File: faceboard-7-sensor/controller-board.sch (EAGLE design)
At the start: 11 parts

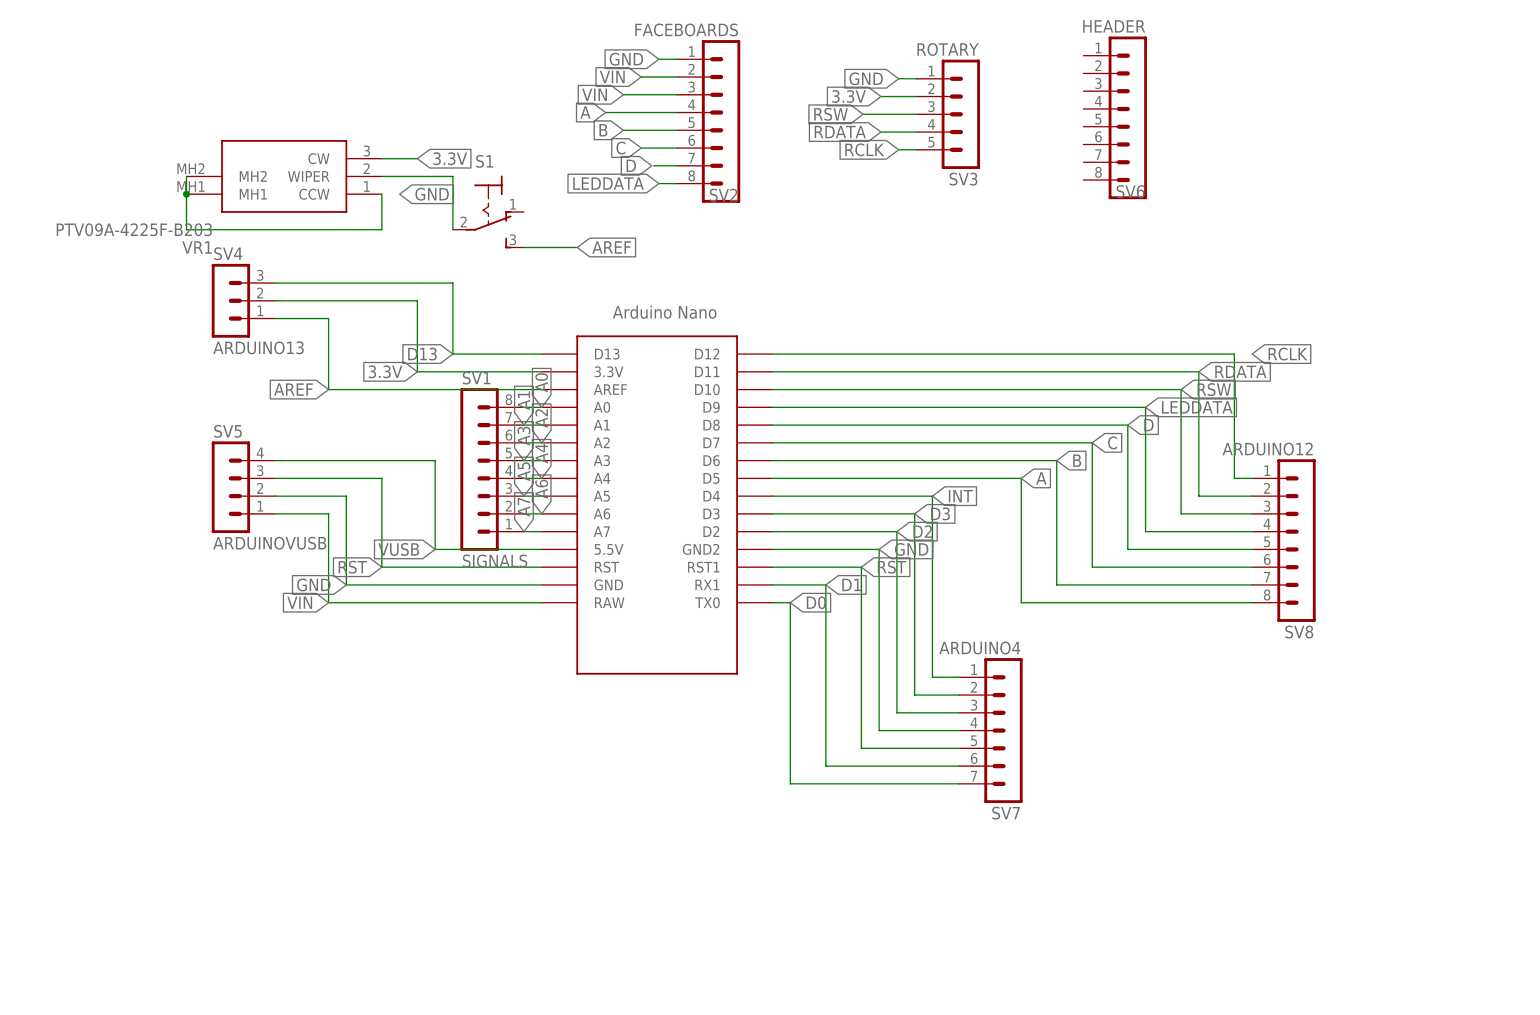
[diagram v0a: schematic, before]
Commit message: add ffc boards
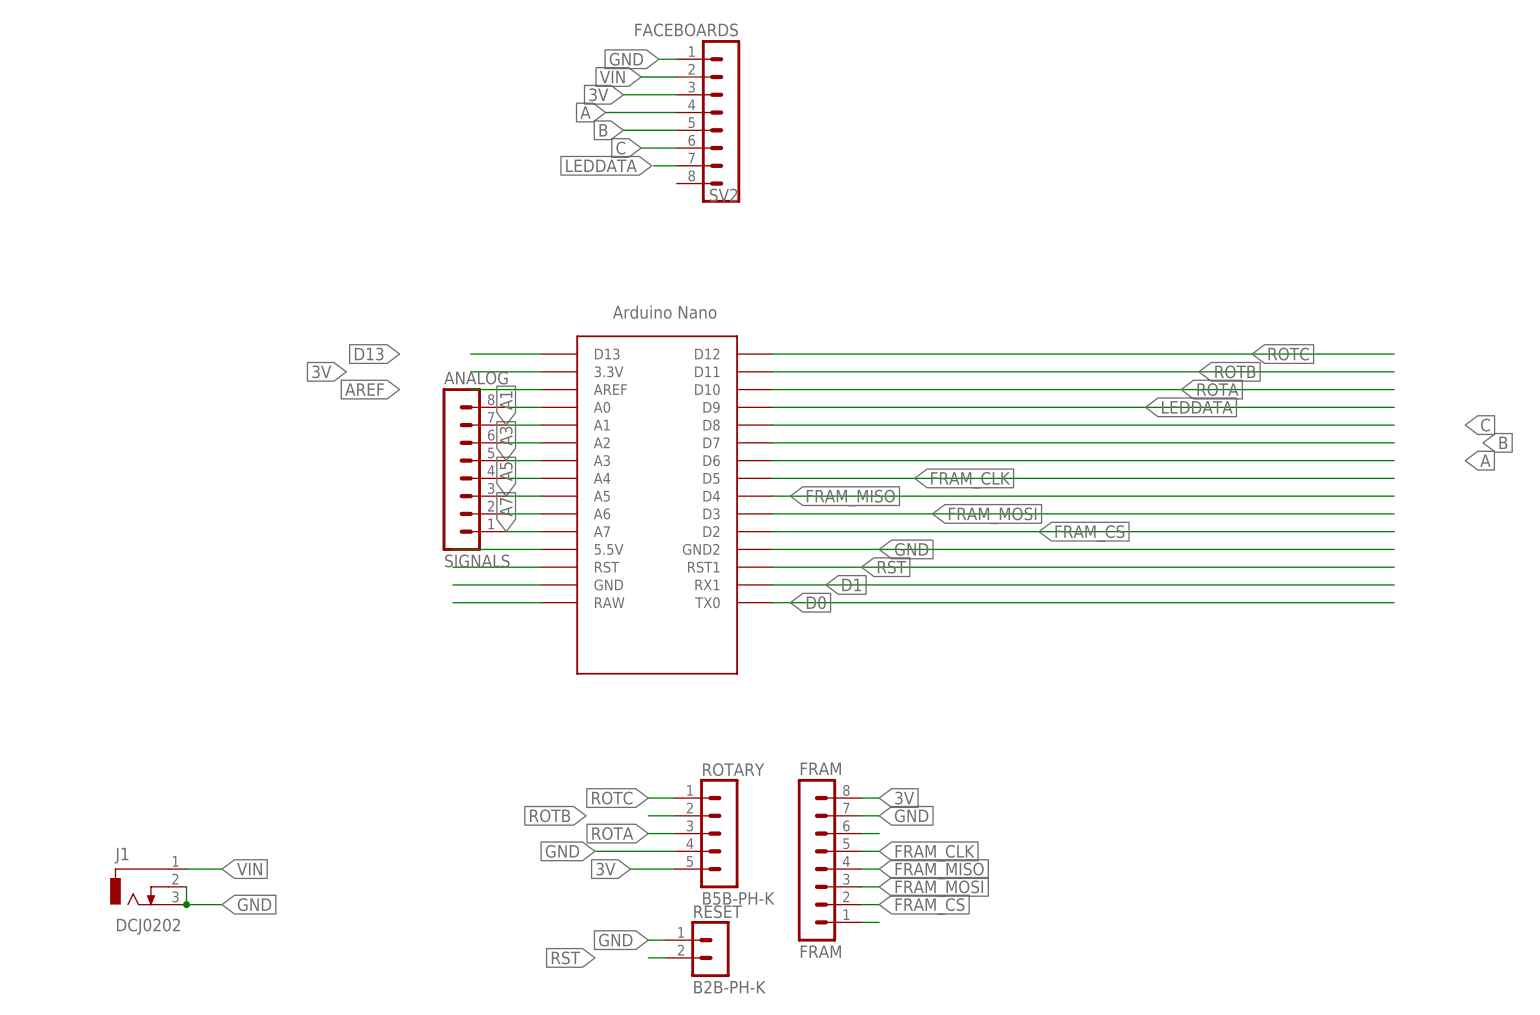
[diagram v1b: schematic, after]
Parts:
- removed S1: (no value), switch:320-916
- removed SV1: SIGNALS, con-lstb:MA08-1
- removed SV3: ROTARY, con-lstb:MA05-1
- removed SV4: ARDUINO13, con-lstb:MA03-1
- removed SV5: ARDUINOVUSB, con-lstb:MA04-1
- removed SV6: HEADER, con-lstb:MA08-1
- removed SV7: ARDUINO4, con-lstb:MA07-1
- removed SV8: ARDUINO12, con-lstb:MA08-1
- removed VR1: PTV09A-4225F-B203, PTV09A-4225F-B203:PTV09A-4225F-B203
- added ANALOG: SIGNALS, con-lstb:MA08-1
- added FRAM: FRAM, con-lstb:MA08-1
- added J1: DCJ0202, con-jack:DCJ0202
- added RESET: B2B-PH-K, con-jst-ph:B2B-PH-K
- added ROTARY: B5B-PH-K, con-jst-ph:B5B-PH-K
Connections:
- removed net 3.3V: SV3.2, SV4.2, U$1.3.3V, VR1.CW
- removed net D: SV2.7, SV8.5, U$1.D8
- removed net D2: SV7.3, U$1.D2
- removed net D3: SV7.2, U$1.D3
- removed net INT: SV7.1, U$1.D4
- removed net N$10: S1.P, VR1.WIPER
- removed net RCLK: SV3.5, SV8.1, U$1.D12
- removed net RDATA: SV3.4, SV8.2, U$1.D11
- removed net RSW: SV3.3, SV8.3, U$1.D10
- new net 3V: FRAM.8, ROTARY.5, SV2.3, U$1.3.3V
- new net FRAM_CLK: FRAM.5, U$1.D5
- new net FRAM_CS: FRAM.2, U$1.D2
- new net FRAM_MISO: FRAM.4, U$1.D4
- new net FRAM_MOSI: FRAM.3, U$1.D3
- new net N$3: FRAM.6
- new net N$8: FRAM.1
- new net ROTA: ROTARY.3, U$1.D10
- new net ROTB: ROTARY.2, U$1.D11
- new net ROTC: ROTARY.1, U$1.D12
- net A: now also U$1.D6; no longer SV8.8, U$1.D5
- net A0: now also ANALOG.8; no longer SV1.8
- net A1: now also ANALOG.7; no longer SV1.7
- net A2: now also ANALOG.6; no longer SV1.6
- net A3: now also ANALOG.5; no longer SV1.5
- net A4: now also ANALOG.4; no longer SV1.4
- net A5: now also ANALOG.3; no longer SV1.3
- net A6: now also ANALOG.2; no longer SV1.2
- net A7: now also ANALOG.1; no longer SV1.1
- net AREF: no longer S1.S, SV4.1
- net B: now also U$1.D7; no longer SV8.7, U$1.D6
- net C: now also U$1.D8; no longer SV8.6, U$1.D7
- net D0: no longer SV7.7
- net D1: no longer SV7.6
- net D13: no longer SV4.3
- net GND: now also FRAM.7, J1.2, J1.3, RESET.1, ROTARY.4; no longer SV3.1, SV5.2, SV7.4, VR1.CCW, VR1.MH1, VR1.MH2
- net LEDDATA: now also SV2.7; no longer SV2.8, SV8.4
- net RST: now also RESET.2; no longer SV5.3, SV7.5
- net VIN: now also J1.1; no longer SV2.3, SV5.1
- net VUSB: no longer SV5.4

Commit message: redraw schematics
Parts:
- SV2: value FACEBOARDS -> SENSOR_BOARD
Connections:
- net FRAM_CLK renamed CLK
- net FRAM_CS renamed CS
- net FRAM_MISO renamed MISO
- net FRAM_MOSI renamed MOSI
- net LEDDATA renamed DIN
- net ROTA renamed RA
- net ROTB renamed RB
- net ROTC renamed RC
- net VIN renamed VCC
- removed net AREF: U$1.AREF
- removed net D0: U$1.TX0
- removed net D1: U$1.RX1
- removed net D13: U$1.D13
- removed net N$3: FRAM.6
- removed net N$8: FRAM.1
- removed net VUSB: U$1.5.5V
- net A0: now also ANALOG.1; no longer ANALOG.8
- net A1: now also ANALOG.2; no longer ANALOG.7
- net A2: now also ANALOG.3; no longer ANALOG.6
- net A3: now also ANALOG.4; no longer ANALOG.5
- net A4: now also ANALOG.5; no longer ANALOG.4
- net A5: now also ANALOG.6; no longer ANALOG.3
- net A6: now also ANALOG.7; no longer ANALOG.2
- net A7: now also ANALOG.8; no longer ANALOG.1
- net GND: no longer U$1.GND
- net RST: no longer U$1.RST1
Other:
- moved on the sheet: J1, RESET, ROTARY
